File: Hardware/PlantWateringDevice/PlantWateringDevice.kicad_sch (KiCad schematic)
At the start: 0 parts

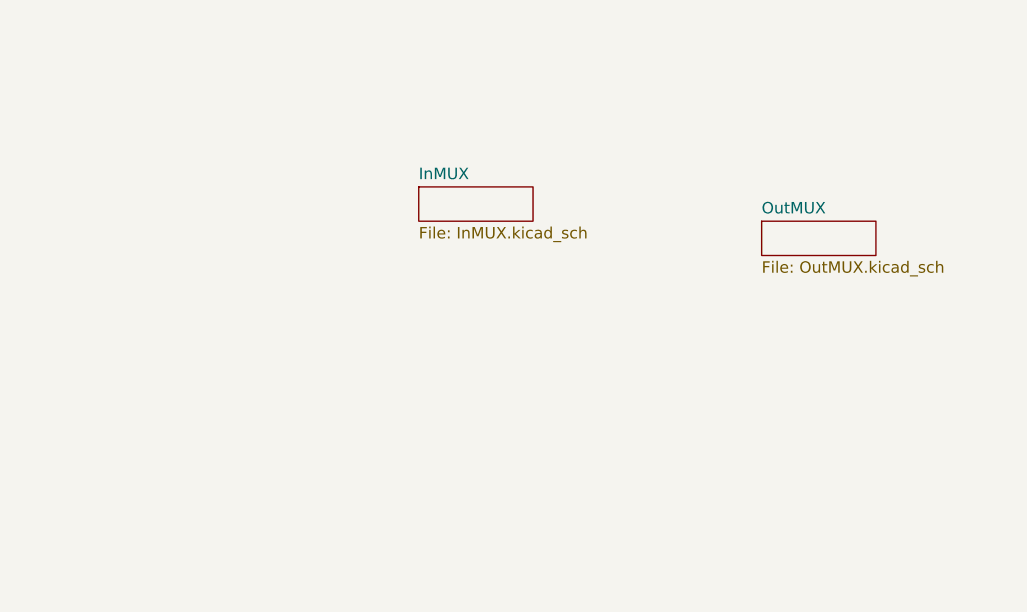
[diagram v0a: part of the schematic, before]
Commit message: circuit simplification
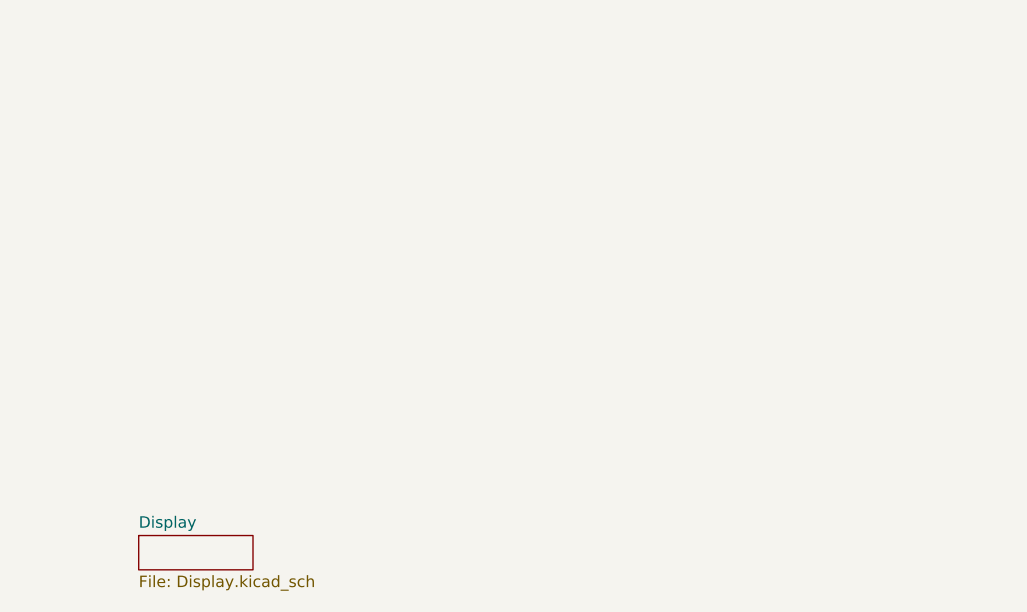
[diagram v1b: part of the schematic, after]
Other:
- removed sheet InMUX
- removed sheet OutMUX
- added sheet Display (Display.kicad_sch)
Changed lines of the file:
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@@
-	)
-	(sheet
-		(at 168.275 98.425)
-		(size 12.7 3.81)
-		(exclude_from_sim no)
-		(in_bom yes)
-		(on_board yes)
-		(dnp no)
-		(fields_autoplaced yes)
-		(stroke
-			(width 0.1524)
-			(type solid)
-		)
-		(fill
-			(color 0 0 0 0.0000)
-		)
-		(property "Sheetname" "OutMUX"
-			(at 168.275 97.7134 0)
-			(effects
-				(font
-					(size 1.27 1.27)
-				)
-				(justify left bottom)
-			)
-		)
-		(property "Sheetfile" "OutMUX.kicad_sch"
-			(at 168.275 102.8196 0)
-			(effects
-				(font
-					(size 1.27 1.27)
-				)
-				(justify left top)
-			)
-		)
-		(instances
-			(project "PlantWateringDevice"
-				(path "/1ef241b3-83d7-48ae-bcca-b7d0eea44e63"
-					(page "7")
-				)
-			)
-		)
 	)
 	(sheet
@@
 	)
 	(sheet
-		(at 130.175 94.615)
+		(at 99.06 133.35)
 		(size 12.7 3.81)
 		(exclude_from_sim no)
@@
 			(color 0 0 0 0.0000)
 		)
-		(property "Sheetname" "InMUX"
-			(at 130.175 93.9034 0)
+		(property "Sheetname" "Display"
+			(at 99.06 132.6384 0)
 			(effects
 				(font
@@
 			)
 		)
-		(property "Sheetfile" "InMUX.kicad_sch"
-			(at 130.175 99.0096 0)
+		(property "Sheetfile" "Display.kicad_sch"
+			(at 99.06 137.7446 0)
 			(effects
 				(font
@@
 			(project "PlantWateringDevice"
 				(path "/1ef241b3-83d7-48ae-bcca-b7d0eea44e63"
-					(page "6")
+					(page "8")
 				)
 			)

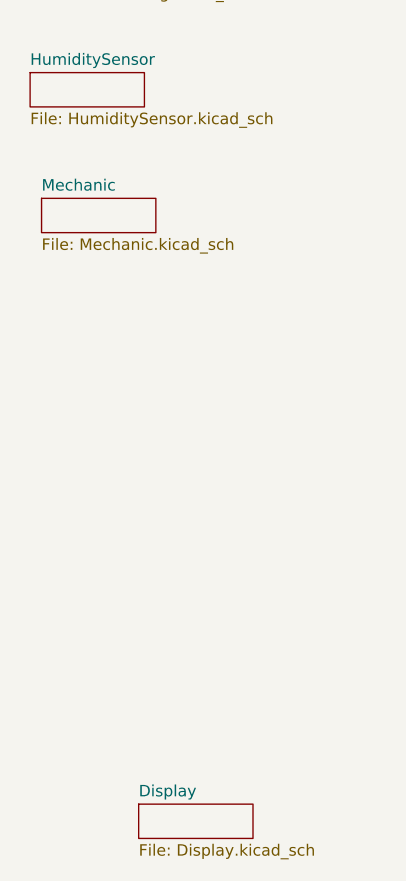
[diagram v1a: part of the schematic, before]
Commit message: fix #16, fix #17, fix #18, fix #19, fix #20, fix #26, fix #27, fix #28, fix #30, fix #32, fix#33, fix #34, fix #35, fix #38
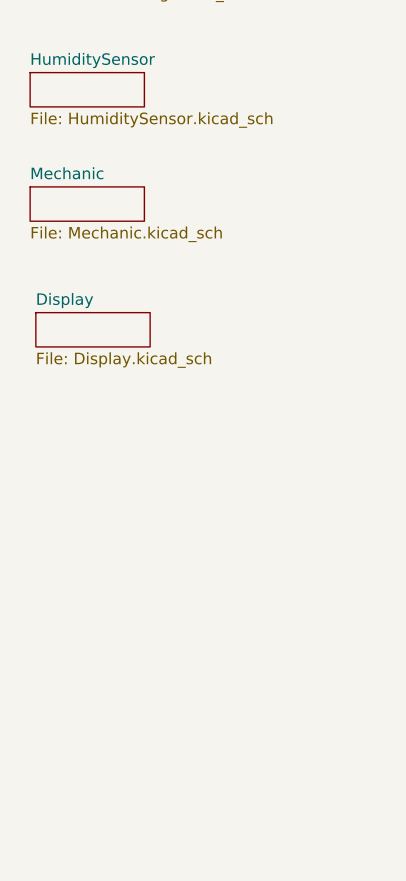
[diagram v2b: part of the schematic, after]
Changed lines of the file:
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@@
 (kicad_sch
-	(version 20250114)
+	(version 20260101)
 	(generator "eeschema")
-	(generator_version "9.0")
+	(generator_version "10.0")
 	(paper "A4")
 	(sheet
@@
 		)
 		(fill
-			(color 0 0 0 0.0000)
+			(color 0 0 0 0)
 		)
 		(property "Sheetname" "PowerManagement"
 			(at 85.725 24.0534 0)
+			(show_name no)
+			(do_not_autoplace no)
 			(effects
 				(font
@@
 		(property "Sheetfile" "PowerManagement.kicad_sch"
 			(at 85.725 29.1596 0)
+			(show_name no)
+			(do_not_autoplace no)
 			(effects
 				(font
@@
 	)
 	(sheet
-		(at 88.265 66.04)
-		(size 12.7 3.81)
-		(exclude_from_sim no)
-		(in_bom yes)
-		(on_board yes)
-		(dnp no)
-		(fields_autoplaced yes)
-		(stroke
-			(width 0.1524)
-			(type solid)
-		)
-		(fill
-			(color 0 0 0 0.0000)
+		(at 86.995 64.77)
+		(size 12.7 3.81)
+		(exclude_from_sim no)
+		(in_bom yes)
+		(on_board yes)
+		(dnp no)
+		(fields_autoplaced yes)
+		(stroke
+			(width 0.1524)
+			(type solid)
+		)
+		(fill
+			(color 0 0 0 0)
 		)
 		(property "Sheetname" "Mechanic"
-			(at 88.265 65.3284 0)
+			(at 86.995 64.0584 0)
+			(show_name no)
+			(do_not_autoplace no)
 			(effects
 				(font
@@
 		)
 		(property "Sheetfile" "Mechanic.kicad_sch"
-			(at 88.265 70.4346 0)
+			(at 86.995 69.1646 0)
+			(show_name no)
+			(do_not_autoplace no)
 			(effects
 				(font
@@
 		)
 		(fill
-			(color 0 0 0 0.0000)
+			(color 0 0 0 0)
 		)
 		(property "Sheetname" "DataHandling"
 			(at 86.36 37.3884 0)
+			(show_name no)
+			(do_not_autoplace no)
 			(effects
 				(font
@@
 		(property "Sheetfile" "DataHandling.kicad_sch"
 			(at 86.36 42.4946 0)
+			(show_name no)
+			(do_not_autoplace no)
 			(effects
 				(font
@@
 		)
 		(fill
-			(color 0 0 0 0.0000)
+			(color 0 0 0 0)
 		)
 		(property "Sheetname" "HumiditySensor"
 			(at 86.995 51.3584 0)
+			(show_name no)
+			(do_not_autoplace no)
 			(effects
 				(font
@@
 		(property "Sheetfile" "HumiditySensor.kicad_sch"
 			(at 86.995 56.4646 0)
+			(show_name no)
+			(do_not_autoplace no)
 			(effects
 				(font
@@
 	)
 	(sheet
-		(at 99.06 133.35)
-		(size 12.7 3.81)
-		(exclude_from_sim no)
-		(in_bom yes)
-		(on_board yes)
-		(dnp no)
-		(fields_autoplaced yes)
-		(stroke
-			(width 0.1524)
-			(type solid)
-		)
-		(fill
-			(color 0 0 0 0.0000)
+		(at 87.63 78.74)
+		(size 12.7 3.81)
+		(exclude_from_sim no)
+		(in_bom yes)
+		(on_board yes)
+		(dnp no)
+		(fields_autoplaced yes)
+		(stroke
+			(width 0.1524)
+			(type solid)
+		)
+		(fill
+			(color 0 0 0 0)
 		)
 		(property "Sheetname" "Display"
-			(at 99.06 132.6384 0)
+			(at 87.63 78.0284 0)
+			(show_name no)
+			(do_not_autoplace no)
 			(effects
 				(font
@@
 		)
 		(property "Sheetfile" "Display.kicad_sch"
-			(at 99.06 137.7446 0)
-			(effects
-				(font
+			(at 87.63 83.1346 0)
+			(show_name no)
+			(do_not_autoplace no)
+			(effects
+				(font

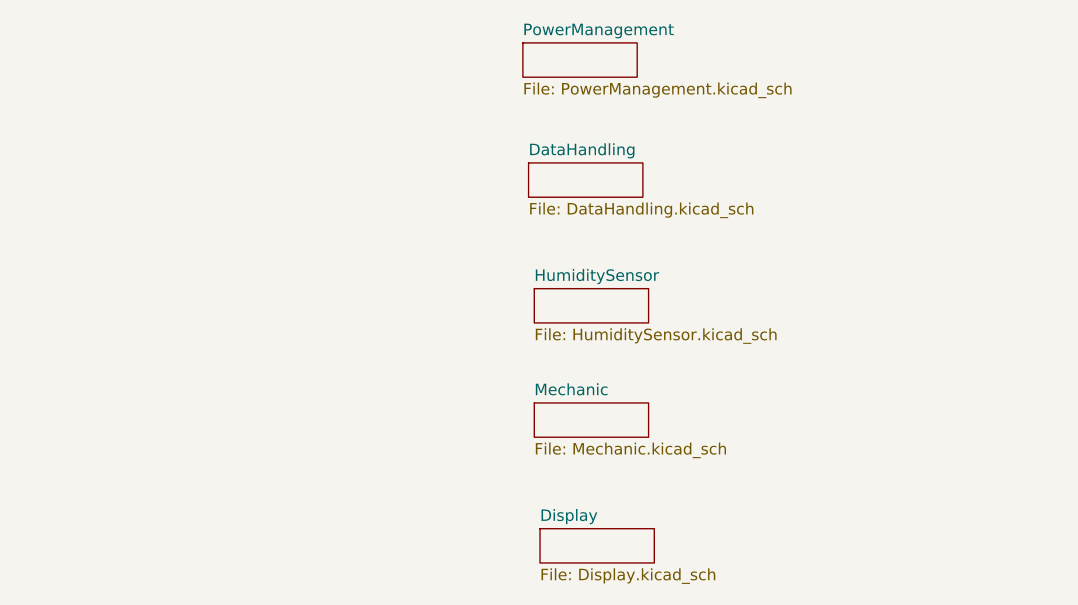
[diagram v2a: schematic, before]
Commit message: hierarchical block diagram structure in kicad
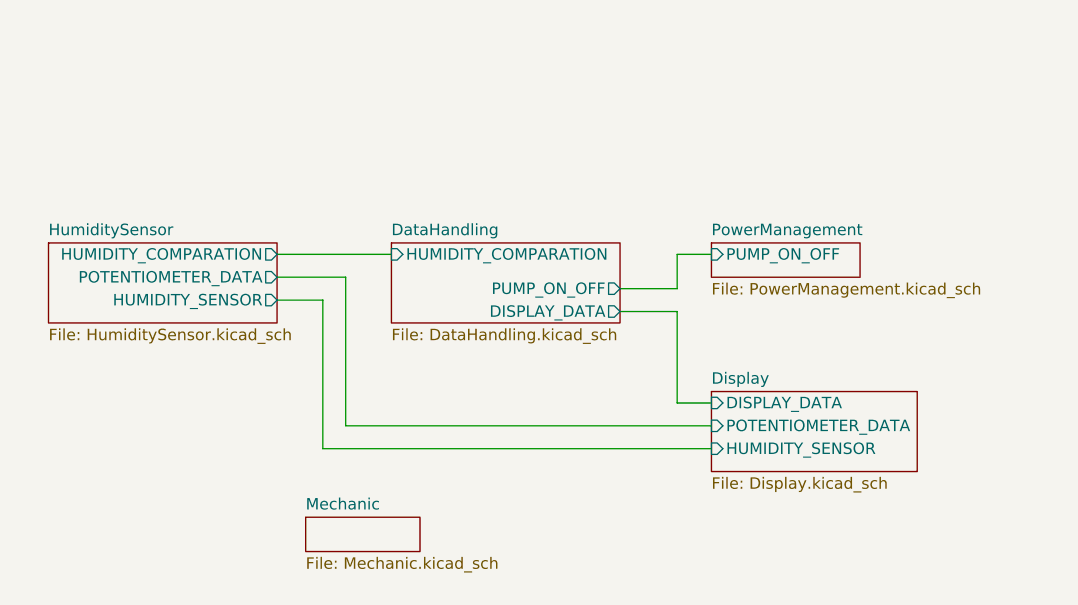
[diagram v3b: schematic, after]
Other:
- sheet DataHandling ports: added DISPLAY_DATA, HUMIDITY_COMPARATION, PUMP_ON_OFF; removed none
- sheet Display ports: added DISPLAY_DATA, HUMIDITY_SENSOR, POTENTIOMETER_DATA; removed none
- sheet HumiditySensor ports: added HUMIDITY_COMPARATION, HUMIDITY_SENSOR, POTENTIOMETER_DATA; removed none
- sheet PowerManagement ports: added PUMP_ON_OFF; removed none
